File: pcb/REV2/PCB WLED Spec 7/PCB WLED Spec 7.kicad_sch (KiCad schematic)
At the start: 22 parts, among them J1 USB_C_Receptacle_USB2.0_16P, U1 ESP32-C3, U2 RT9013-33GB

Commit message: eddited pcb rev2 and logboek update
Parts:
- added C10, C11, C8, C9: C47µF, Capacitor_SMD:C_1206_3216Metric, symbol Device:C
- added L2: L10µH, symbol Device:L
- added R10: R17.8k, symbol Device:R
- added R11: R84.5k, symbol Device:R
- added R9: R100k, symbol Device:R
- added U3: LMR14050SDDAR, LMR14050SDDAR:VREG_LM5017MR_NOPB, symbol LMR14050SDDAR:LMR14050SDDAR
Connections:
- net 5V_BUCK: now also C10.1, C11.1, C8.1, C9.1, L2.2, R9.2
- net GND: now also C10.2, C11.2, C8.2, C9.2, R10.2, R11.2, U3.10 (EXP), U3.11 (EXP), U3.12 (EXP), U3.13 (EXP), U3.14 (EXP), U3.15 (EXP), U3.16 (EXP), U3.17 (EXP), U3.7 (GND), U3.9 (EXP)
- new net: L2.1, U3.8 (SW)
- new net FB: R10.1, R9.1, U3.5 (FB)
- new net Switching frequency: R11.1, U3.4 (RT/SYNC)
- no-connect marks 9 -> 10

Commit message: update pcb rev 2
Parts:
- added C12, C14: C0.1µF, symbol Device:C
- added C13: C22nF, symbol Device:C
- added C15, C16: C4.7µF, symbol Device:C
- added D2: D_Schottky, STPS5L60S:DIOM6859X262N, symbol Device:D_Schottky
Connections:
- net +BATT: now also U3.2 (VIN), C14.1, C15.1, C16.1
- net GND: now also C13.2, C14.2, C15.2, C16.2, D2.2 (A)
- net at L2.1, U3.8 (SW): now also C12.2, D2.1 (K)
- net at U3.1 (BOOT): now also C12.1
- net SS: now reaches U3.6 (SS)
- net SS: now also C13.1
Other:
- moved on the sheet: C10, C11, C8, C9, L2, R10, R9

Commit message: pcb rev2 update
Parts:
- added AE1: 2450AT18A100E, 2450AT18A100E:ANTC3216X140N, symbol 2450AT18A100E:2450AT18A100E
- added Q1, Q2: BC807, Package_TO_SOT_SMD:SOT-23, symbol Transistor_BJT:BC807
- added R12, R13, R14, R15: R1k, Resistor_SMD:R_0402_1005Metric, symbol Device:R
- C1, C12, C13, C14, C2, C3, C4, C5, C7: footprint (none) -> Capacitor_SMD:C_0402_1005Metric
- C6: footprint (none) -> Capacitor_SMD:C_0603_1608Metric
- L1: footprint (none) -> Inductor_SMD:L_0603_1608Metric
- R10, R11, R5, R6, R7, R8, R9: footprint (none) -> Resistor_SMD:R_0402_1005Metric
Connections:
- net 5V_BUCK: now also Q1.2 (E), Q2.2 (E)
- net GND: now also R13.1, R15.1
- net WIFI_ANT: now also AE1.1
- net LED1_IN: now reaches R5.1, U1.6 (GPIO2)
- net LED1_IN: now also R12.1
- net LED2_IN: now reaches U1.16 (GPIO10)
- net LED2_IN: now also R14.1
- new net: Q2.1 (B), R14.2
- new net: Q1.1 (B), R12.2
- new net LED1_OUT: Q1.3 (C), R13.2
- new net LED2_OUT: Q2.3 (C), R15.2
- no-connect marks 10 -> 19

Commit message: pcb v2 update
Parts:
- removed Q2: BC807, Package_TO_SOT_SMD:SOT-23, symbol Transistor_BJT:BC807
- removed R14, R15: R1k, Resistor_SMD:R_0402_1005Metric, symbol Device:R
- added S3, S4, S5, S6, S7, S8: solder pad, custom:solder pad small, symbol custom:solder_pad
- added Y1: XRCGB40M000F1S1DR0, XRCGB40M000F1S1DR0:OSC_XRCGB40M000F1S1DR0, symbol XRCGB40M000F1S1DR0:XRCGB40M000F1S1DR0
- C15, C16: footprint (none) -> Capacitor_SMD:C_0805_2012Metric
- L2: footprint (none) -> custom:TECHFUSE SL1050-100M
- R1, R2: footprint (none) -> Resistor_SMD:R_0402_1005Metric
- R3, R4: footprint (none) -> Resistor_SMD:R_0402_1005Metric_Pad0.72x0.64mm_HandSolder
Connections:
- net LED2_IN is gone; now on net LED1_IN: U1.16 (GPIO10)
- net +BATT: now also S3.1 (solder)
- net 5V_BUCK: now also S5.1 (solder)
- net GND: now also S4.1 (solder), S6.1 (solder)
- net LED1_IN: no longer R5.1, U1.6 (GPIO2)
- net LED1_OUT: now also S7.1 (solder)
- new net PWM1: R5.1, S8.1 (solder), U1.6 (GPIO2)

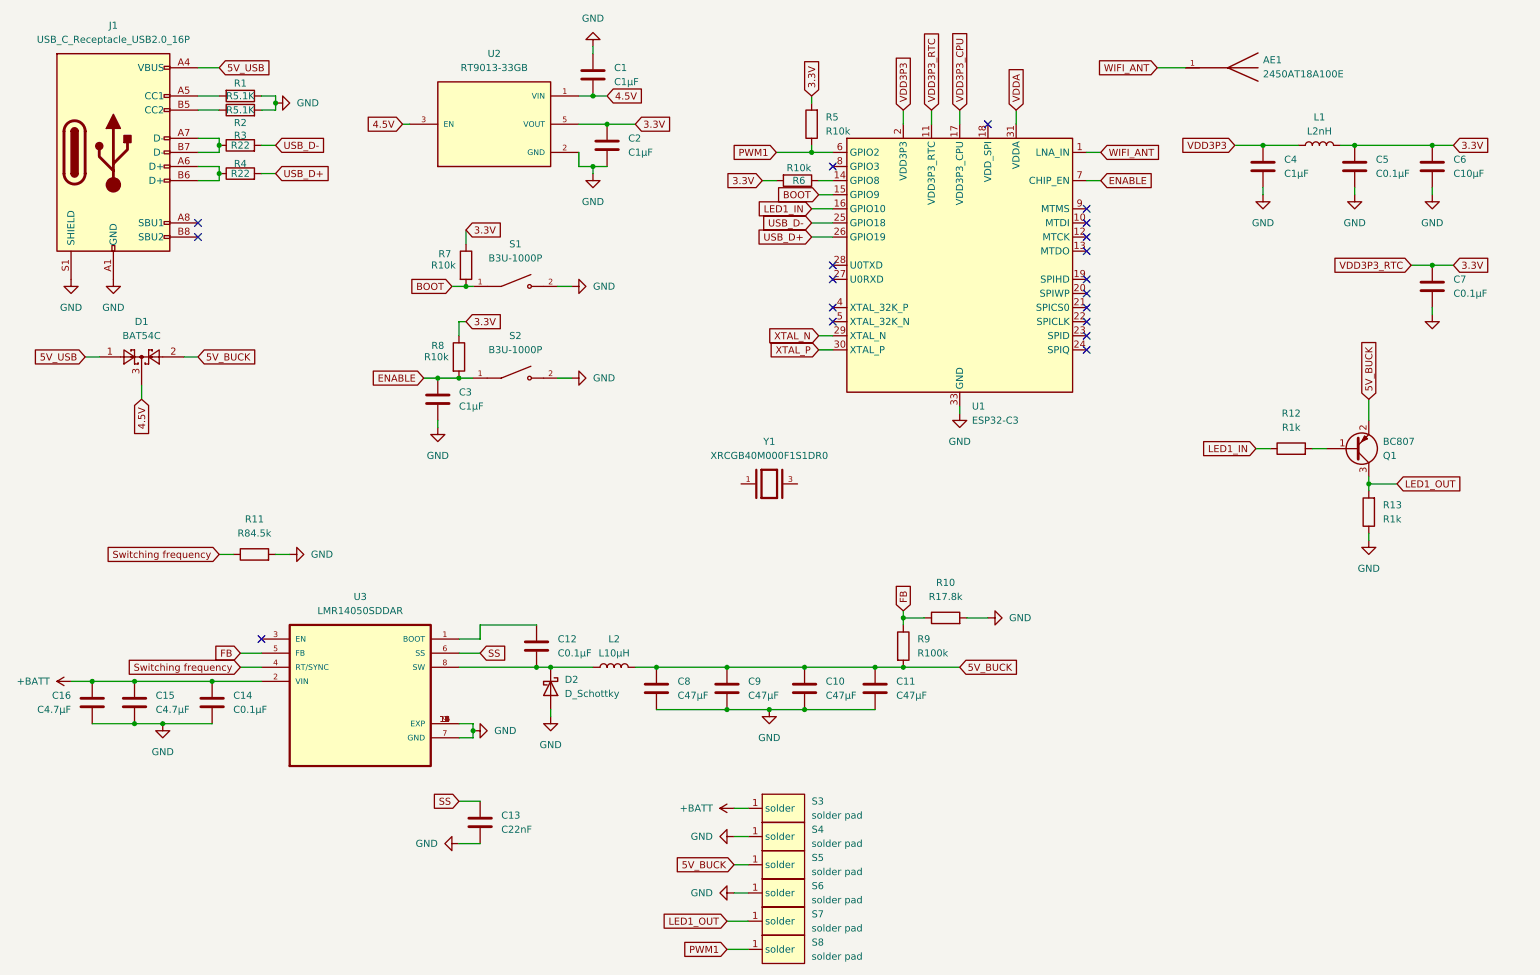
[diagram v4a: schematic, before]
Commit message: pcb layout finished
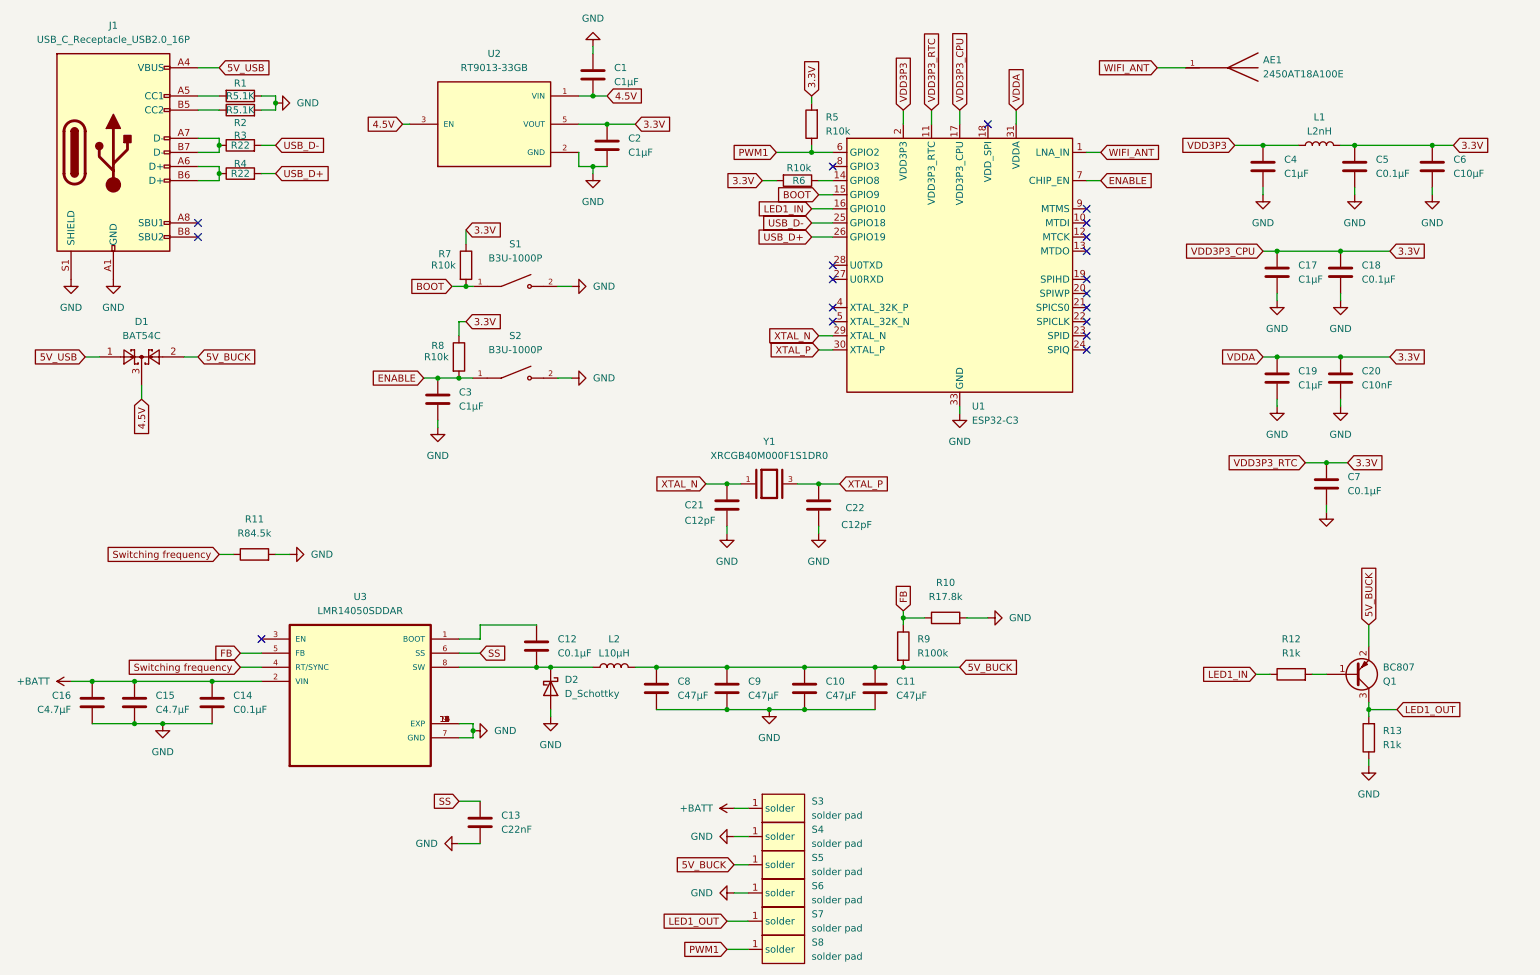
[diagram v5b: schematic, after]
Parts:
- added C17, C19: C1µF, Capacitor_SMD:C_0402_1005Metric, symbol Device:C
- added C18: C0.1µF, Capacitor_SMD:C_0402_1005Metric, symbol Device:C
- added C20: C10nF, Capacitor_SMD:C_0402_1005Metric, symbol Device:C
- added C21, C22: C12pF, Capacitor_SMD:C_0402_1005Metric, symbol Device:C
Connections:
- net VDD3P3_CPU is gone; now on net 3.3V: U1.17 (VDD3P3_CPU)
- net VDDA is gone; now on net 3.3V: U1.31 (VDDA), U1.32 (VDDA)
- net 3.3V: now also C17.1, C18.1, C19.1, C20.1
- net GND: now also C17.2, C18.2, C19.2, C20.2, C21.2, C22.2
- net XTAL_N: now also Y1.1, C21.1
- net XTAL_P: now also Y1.3, C22.1
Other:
- moved on the sheet: C7, Q1, R12, R13
